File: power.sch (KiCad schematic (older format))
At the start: 55 parts, among them J2 Conn_01x02_Male, J3 Conn_01x02_Male, U1 LM66100, U2 LM66100, U3 TLV76750, U4 AP63203WU, U5 MCP73123-22S

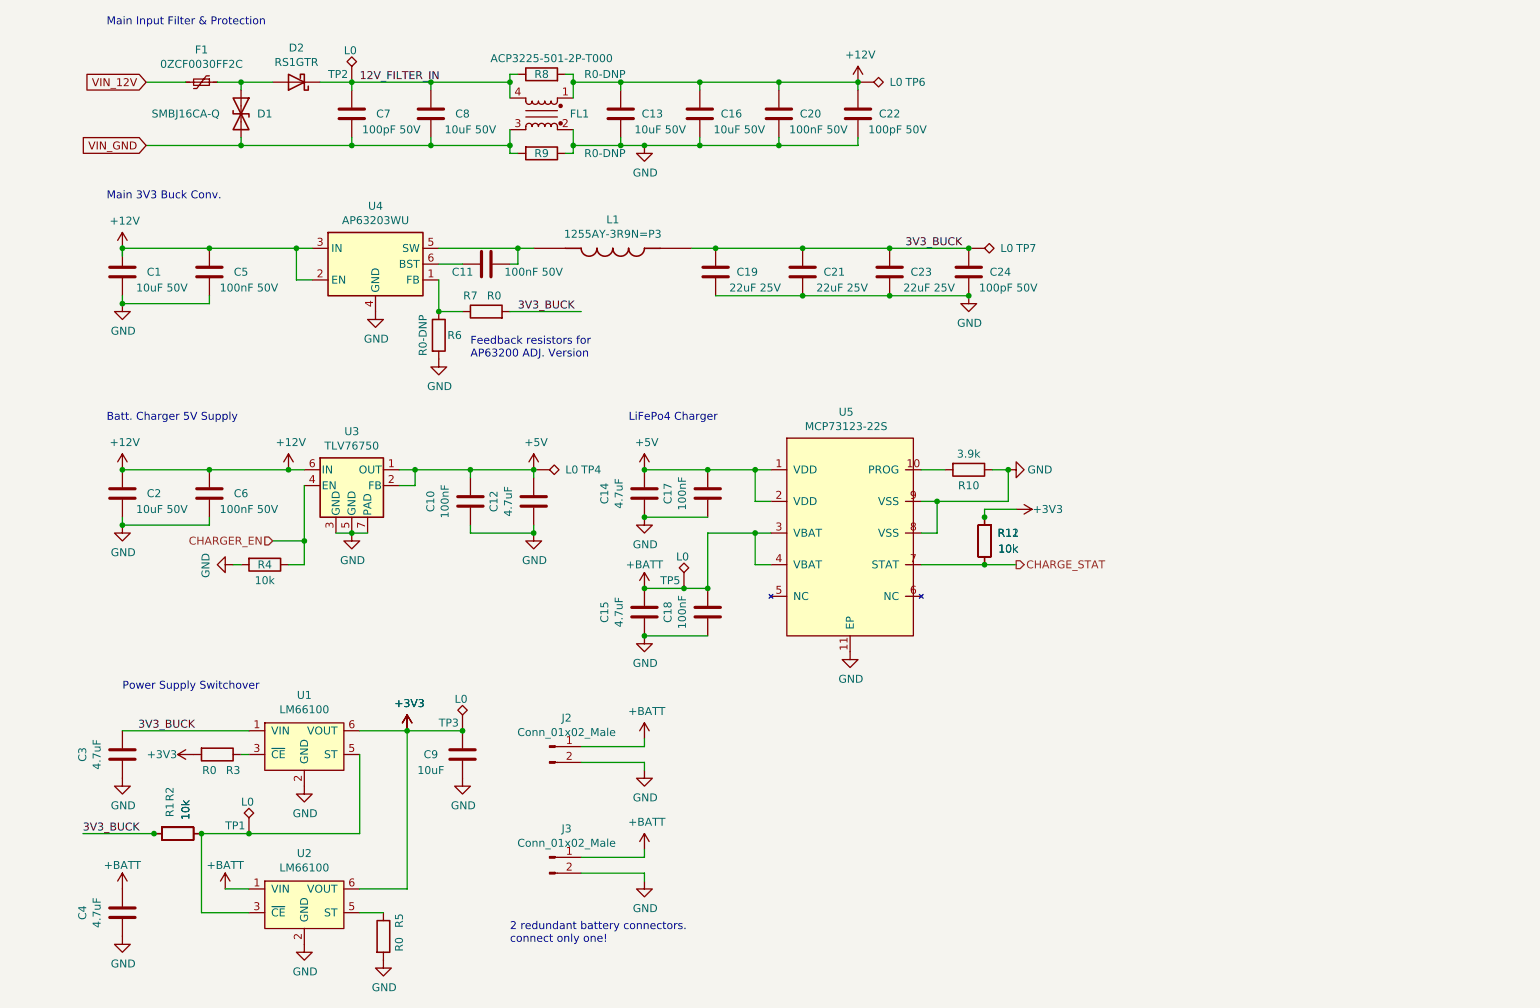
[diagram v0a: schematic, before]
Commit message: Updated power mux with LM73100.
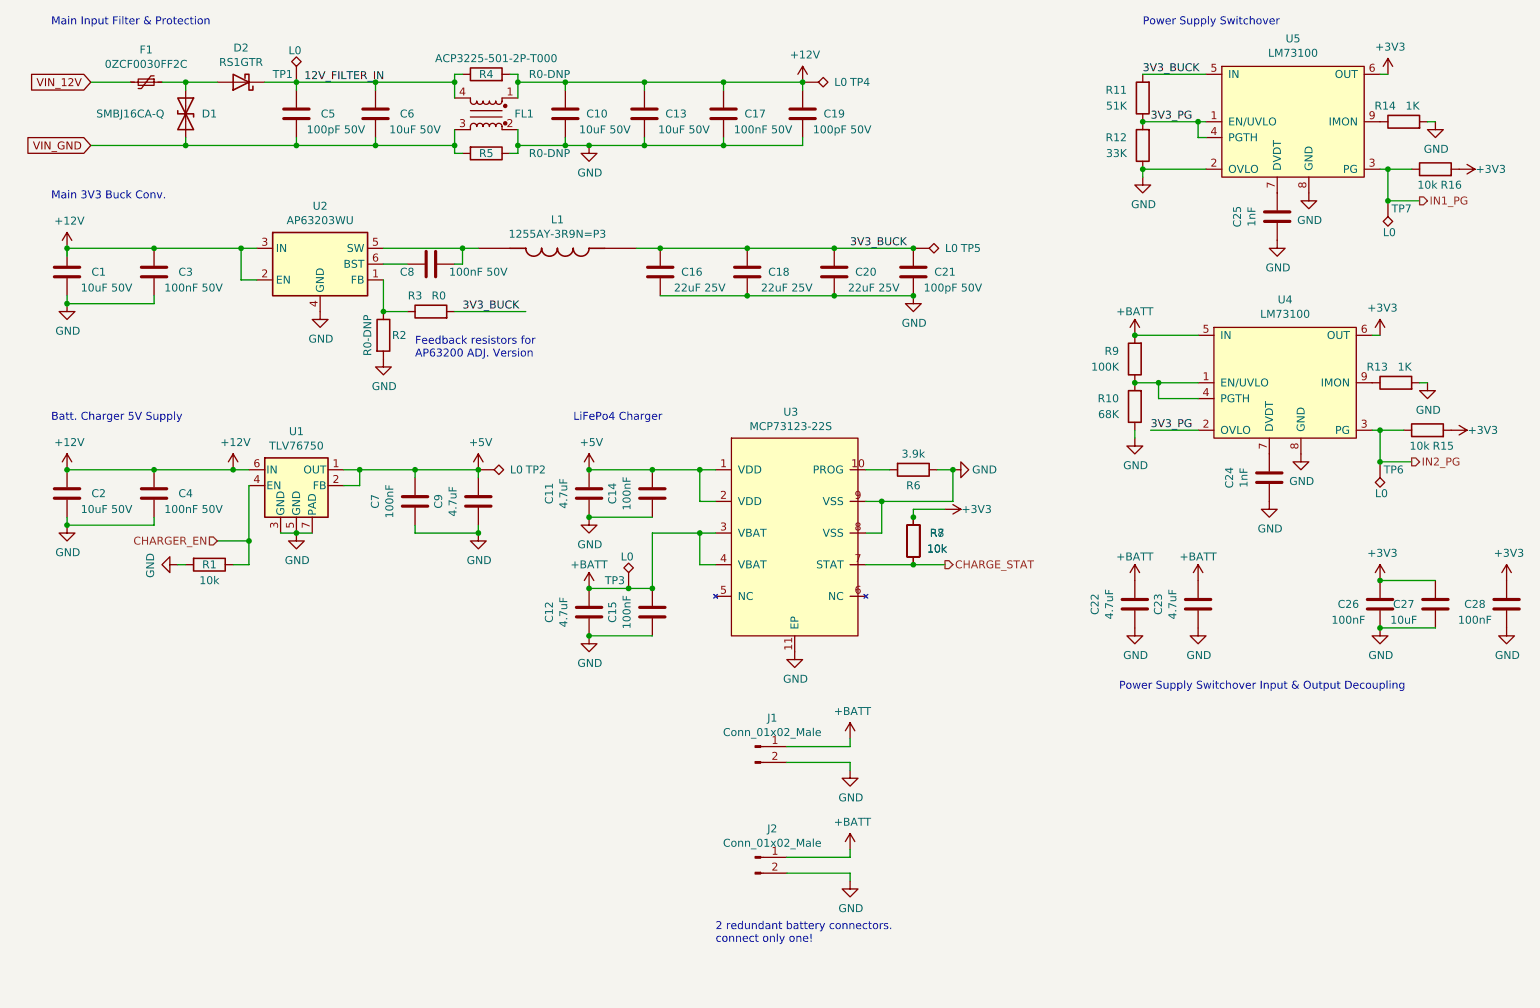
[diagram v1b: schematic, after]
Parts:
- removed C3, C4: 4.7uF, Capacitor_SMD:C_0603_1608Metric, symbol Device:C
- removed C9: 10uF, Capacitor_SMD:C_0603_1608Metric, symbol Device:C
- removed R1, R2: 10k, Resistors:0603, symbol Device:R
- removed R3, R5: R0, Resistors:0603, symbol Device:R
- removed TP1, TP3: L0, OLIMEX_TestPoints-FP:TP_SMD, symbol Connector:TestPoint_Alt
- removed U1, U2: LM66100, Package_TO_SOT_SMD:SOT-363_SC-70-6, symbol pocasicko-cache:Moje_LM66100
- added C22, C23: 4.7uF, Capacitor_SMD:C_0603_1608Metric, symbol Device:C
- added C24, C25: 1nF, Capacitor_SMD:C_0603_1608Metric, symbol Device:C
- added C26, C28: 100nF, Capacitor_SMD:C_0603_1608Metric, symbol Device:C
- added C27: 10uF, Capacitor_SMD:C_0603_1608Metric, symbol Device:C
- added R10: 68K, Resistor_SMD:R_0603_1608Metric, symbol Device:R
- added R11: 51K, Resistor_SMD:R_0603_1608Metric, symbol Device:R
- added R12: 33K, Resistor_SMD:R_0603_1608Metric, symbol Device:R
- added R13, R14: 1K, Resistor_SMD:R_0603_1608Metric, symbol Device:R
- added R15, R16: 10k, Resistors:0603, symbol Device:R
- added R9: 100K, Resistor_SMD:R_0603_1608Metric, symbol Device:R
- added TP6, TP7: L0, OLIMEX_TestPoints-FP:TP_SMD, symbol Connector:TestPoint_Alt
- added U4, U5: LM73100, artanis-light:LM73100, symbol artanis-light-lib:LM73100
- renumbered C13 to C10, C14 to C11, C15 to C12, C16 to C13, C17 to C14, C18 to C15, C19 to C16, C20 to C17, C21 to C18, C22 to C19, C23 to C20, C24 to C21, C5 to C3, C6 to C4, C7 to C5, C8 to C6, C10 to C7, C11 to C8, C12 to C9, J2 to J1, J3 to J2, R4 to R1, R6 to R2, R7 to R3, R8 to R4, R9 to R5, R10 to R6, R11 to R7, R12 to R8, TP2 to TP1, TP4 to TP2, TP5 to TP3, TP6 to TP4, TP7 to TP5, U3 to U1, U4 to U2, U5 to U3
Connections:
- net +3V3: now also C26.1, C27.1, C28.1, R15.2, R16.2, U4.6 (OUT), U5.6 (OUT)
- net +BATT: now also C22.1, C23.1, R9.2, U4.5 (IN)
- net 3V3_BUCK: now also R11.2, U5.5 (IN)
- net GND: now also C22.2, C23.2, C24.2, C25.2, C26.2, C27.2, C28.2, R10.1, R12.1, R13.2, R14.2, U4.8 (GND), U5.2 (OVLO), U5.8 (GND)
- new net: R10.2, R9.1, U4.1 (EN/UVLO), U4.4 (PGTH)
- new net: C24.1, U4.7 (DVDT)
- new net: R13.1, U4.9 (IMON)
- new net: C25.1, U5.7 (DVDT)
- new net: R14.1, U5.9 (IMON)
- new net 3V3_PG: R11.1, R12.2, U4.2 (OVLO), U5.1 (EN/UVLO), U5.4 (PGTH)
- new net IN1_PG: R16.1, TP7.1, U5.3 (PG)
- new net IN2_PG: R15.1, TP6.1, U4.3 (PG)
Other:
- note added: "Power Supply Switchover Input & Output Decoupling"
- moved on the sheet: C1, C10, C11, C12, C13, C14, C15, C16, C17, C18, C19, C2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

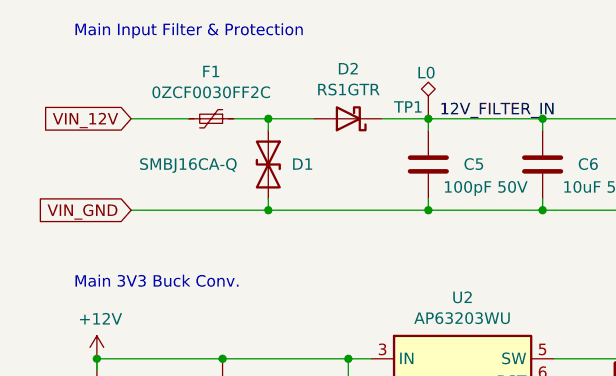
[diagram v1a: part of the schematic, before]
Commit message: Changed PTC Fuse.
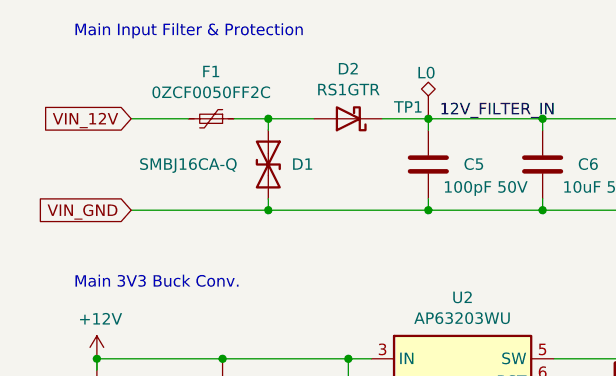
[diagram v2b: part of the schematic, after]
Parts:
- F1: value 0ZCF0030FF2C -> 0ZCF0050FF2C
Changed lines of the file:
@@
 P 1850 1550
 F 0 "F1" V 1645 1550 50  0000 C CNN
-F 1 "0ZCF0030FF2C" V 1736 1550 50  0000 C CNN
+F 1 "0ZCF0050FF2C" V 1736 1550 50  0000 C CNN
 F 2 "Fuse:Fuse_2920_7451Metric_Castellated" H 1900 1350 50  0001 L CNN
 F 3 "~" H 1850 1550 50  0001 C CNN
